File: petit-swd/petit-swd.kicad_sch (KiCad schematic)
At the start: 11 parts, among them CON101 302-S201, CON102 61300411121, CON103 PPTC041LGBN-RC, CON104 USB-B1HSB6, CON105 61300311121, CON106 61300211121, U101 AZ1117CH-3.3TRG1

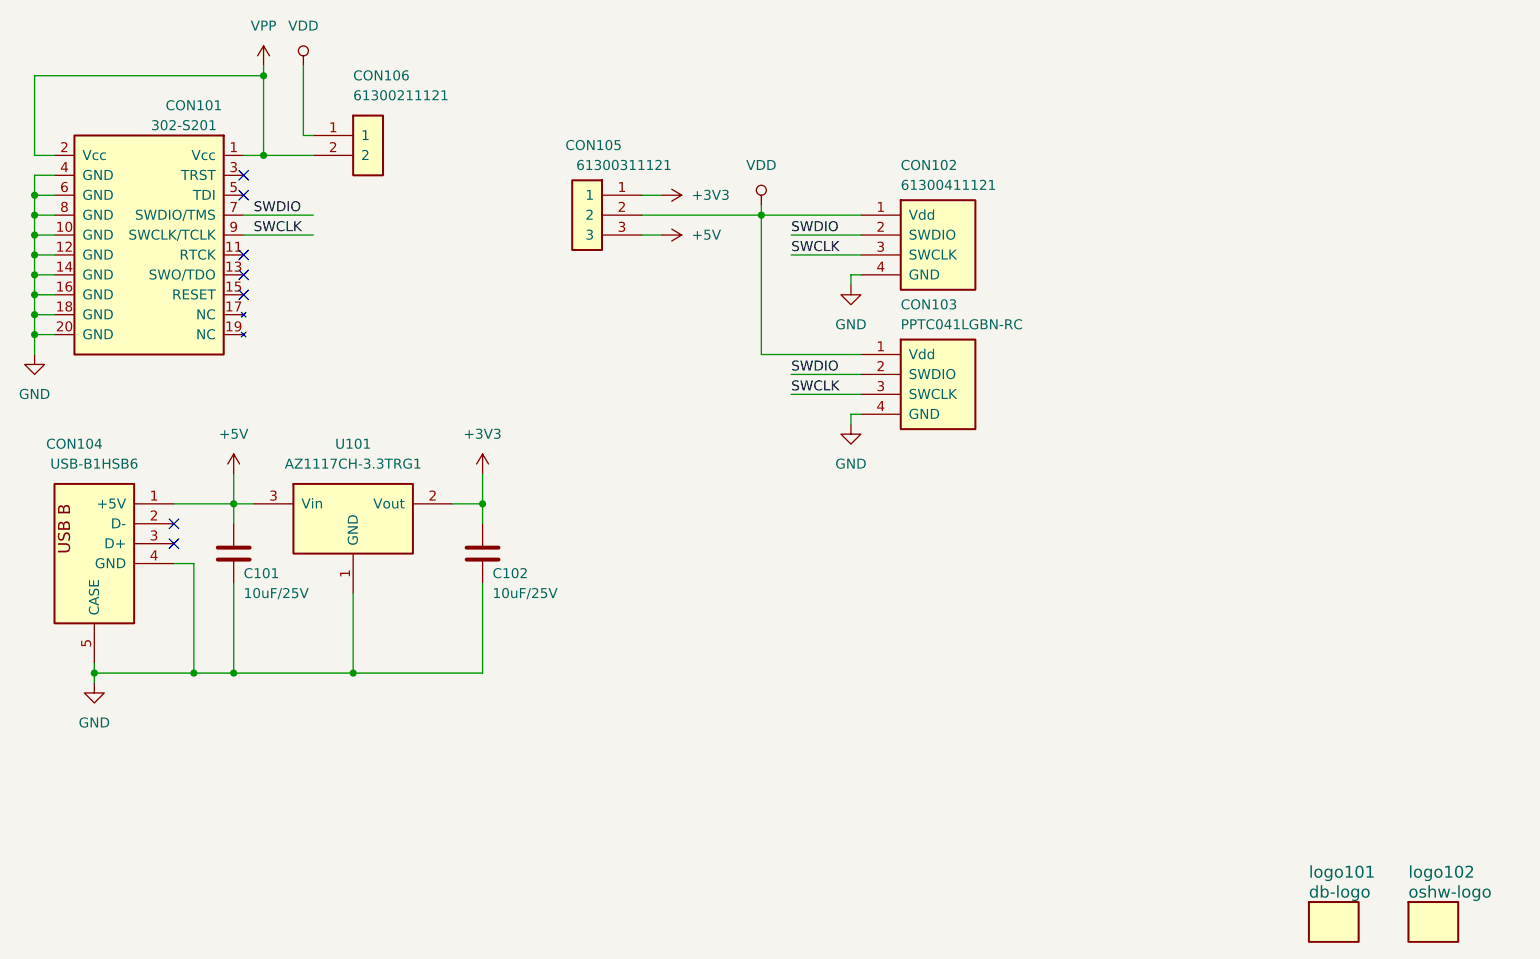
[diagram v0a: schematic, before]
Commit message: swd v1.0 sch complete, jtag v1.1 files
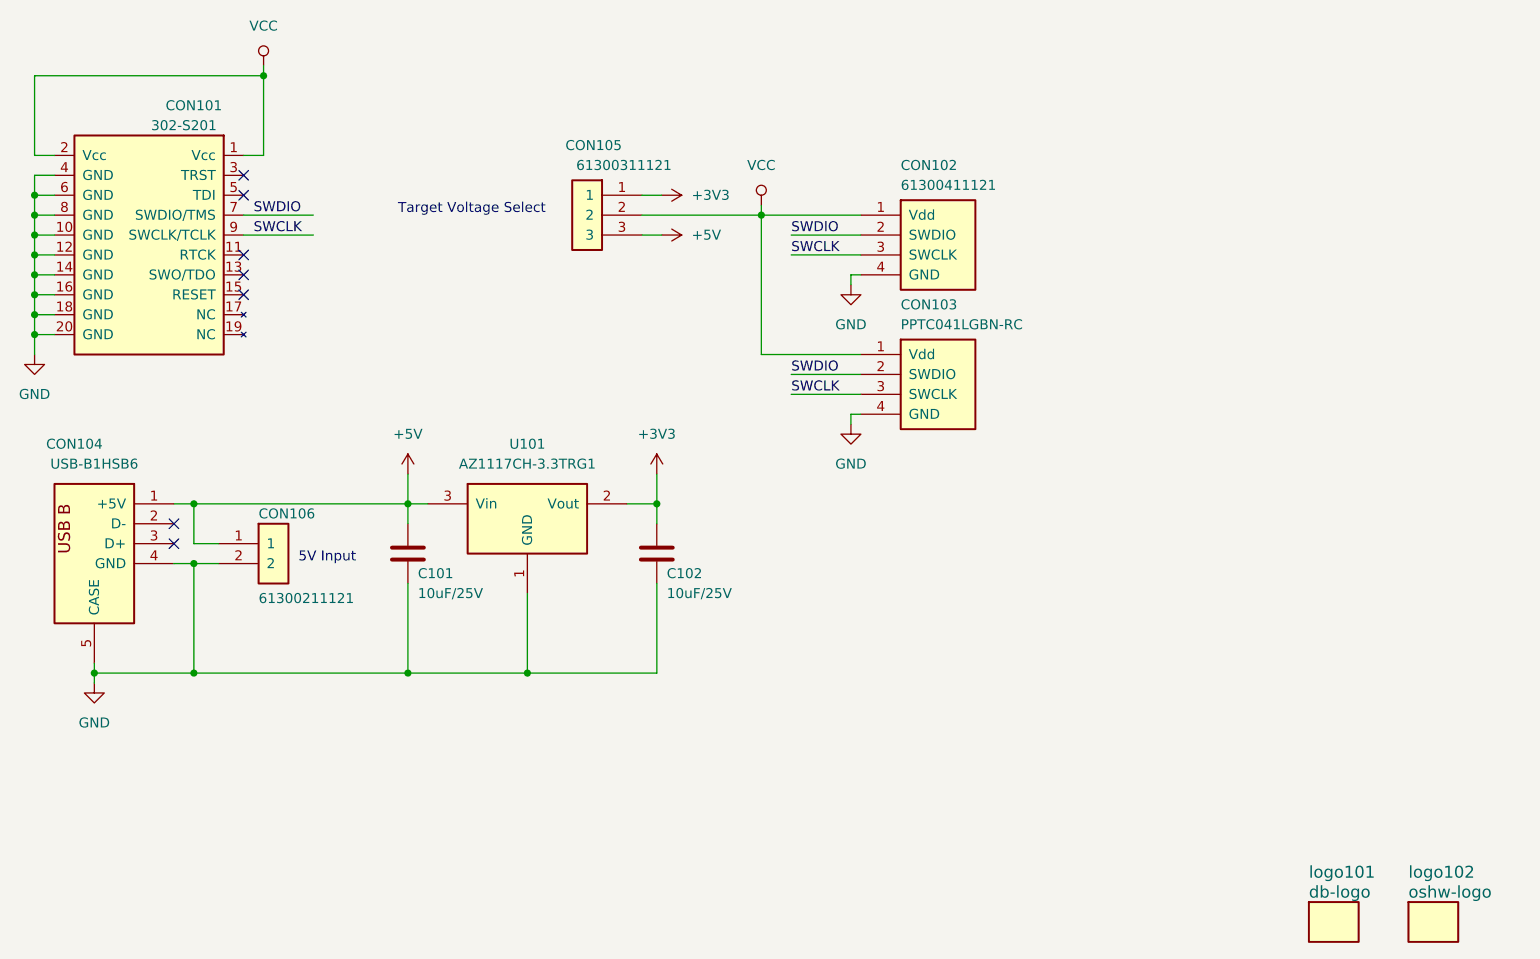
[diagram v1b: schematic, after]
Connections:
- net +5V: now also CON106.1
- net GND: now also CON106.2
- net VDD renamed VCC
- net VCC: now also CON101.1 (Vcc), CON101.2 (Vcc); no longer CON106.1
- removed net VPP: CON101.1 (Vcc), CON101.2 (Vcc), CON106.2
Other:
- note added: "5V Input"
- note added: "Target Voltage Select"
- moved on the sheet: C101, C102, CON106, U101
